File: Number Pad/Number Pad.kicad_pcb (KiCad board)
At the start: 2 copper layers, 92.9 x 95.2 mm, 42 parts, among them J1 Conn_01x19_Female, J2 Conn_01x19_Male

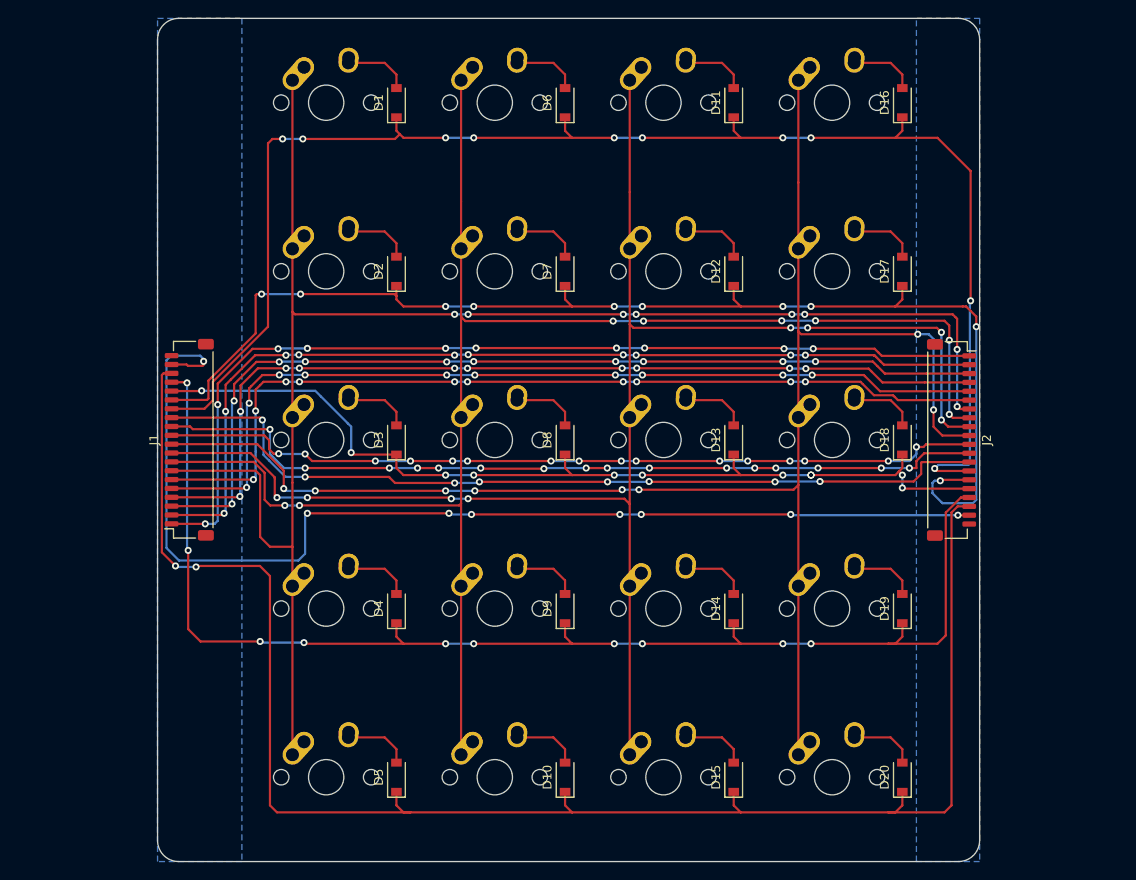
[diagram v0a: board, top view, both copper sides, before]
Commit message: Finished connectors plus mounting holes
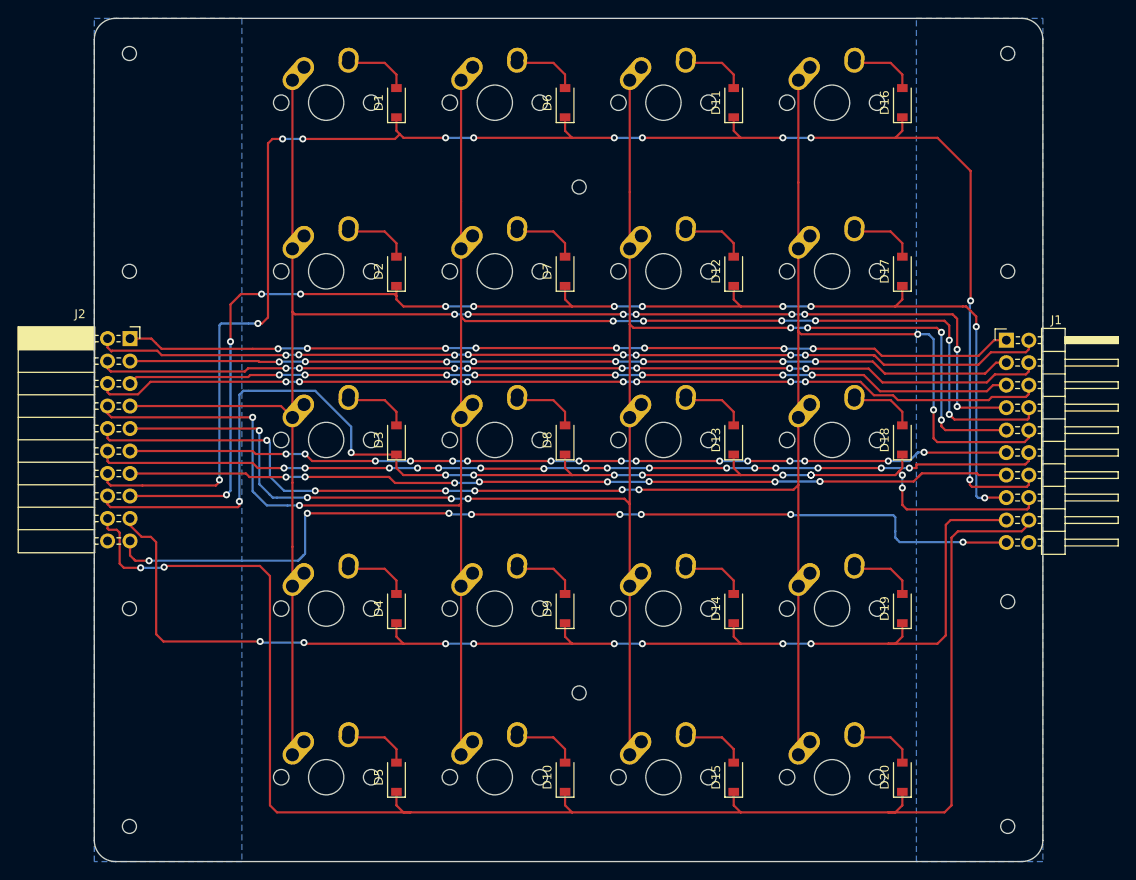
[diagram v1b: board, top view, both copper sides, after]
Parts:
- J1: value Conn_01x19_Female -> Conn_02x10_Counter_Clockwise; footprint Connector_JST:JST_SH_SM20B-SRSS-TB_1x20-1MP_P1.00mm_Horizontal -> Connector_PinHeader_2.54mm:PinHeader_2x10_P2.54mm_Horizontal
- J2: value Conn_01x19_Male -> Conn_02x10_Counter_Clockwise; footprint Connector_JST:JST_SH_SM20B-SRSS-TB_1x20-1MP_P1.00mm_Horizontal -> Connector_PinSocket_2.54mm:PinSocket_2x10_P2.54mm_Horizontal
- moved J2 93.5 mm to (27.9, 51.3), turned to 0 degrees
- moved J1 93.0 mm to (126.8, 51.4), turned to 0 degrees
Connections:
- J1 pad 20: (no net) -> unconnected-(J1-Pad20)
- J2 pad 20: (no net) -> unconnected-(J2-Pad20)
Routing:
- net ROW7: track 105.9 -> 137.1 mm
- net ROW5: track 169.5 -> 192.1 mm, vias 10 -> 12
- net COL5: track 181.1 -> 203.2 mm
- net COL7: track 180.6 -> 199.2 mm
- net GND: track 126.2 -> 109.2 mm
- net COL6: track 180.5 -> 193.4 mm
- net COL9: track 94.9 -> 107.1 mm
- net ROW6: track 141.7 -> 151.6 mm, vias 10 -> 12
- net ROW8: track 144.9 -> 135.9 mm, vias 10 -> 8
- net +5V: track 107.8 -> 100.6 mm, vias 10 -> 8
- net COL8: track 93.1 -> 99.9 mm
- net COL3: track 101.4 -> 107.9 mm, vias 10 -> 8
- net ROW9: track 185.7 -> 179.7 mm
- net COL0: track 104.9 -> 100.1 mm, vias 10 -> 8
- net COL10: track 97.1 -> 100.4 mm
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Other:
- board size 92.9 x 95.2 mm -> 107.2 x 95.2 mm

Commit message: Extended PCB for connectors
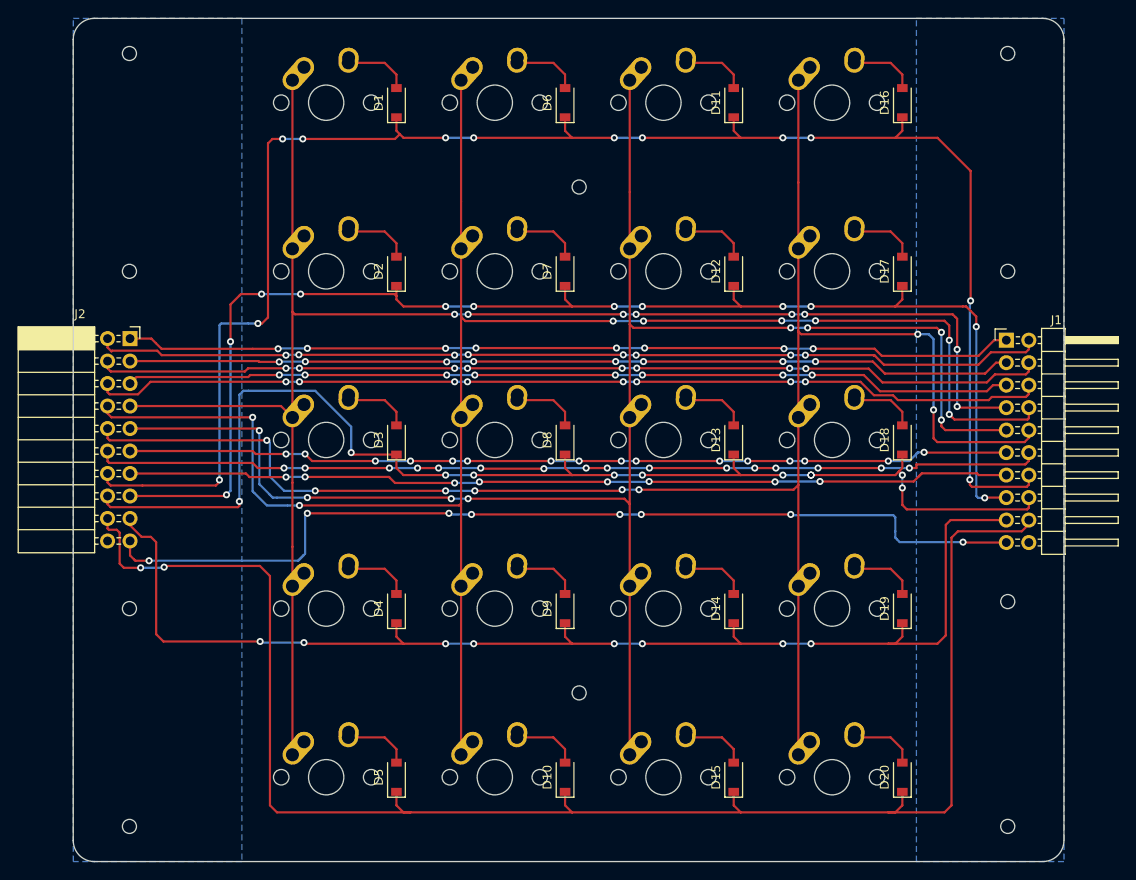
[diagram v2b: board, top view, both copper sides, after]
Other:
- board size 107.2 x 95.2 mm -> 111.9 x 95.2 mm
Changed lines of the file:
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@@
     )
   )
-  (gr_arc (start 128.5875 15.08125) (mid 130.271298 15.778702) (end 130.96875 17.4625) (layer "Edge.Cuts") (width 0.15))
   (gr_circle (center 27.78125 19.05) (end 28.575 19.05) (layer "Edge.Cuts") (width 0.1) (fill none))
   (gr_circle (center 78.58125 34.13125) (end 78.58125 33.3375) (layer "Edge.Cuts") (width 0.1) (fill none))
-  (gr_line (start 23.8125 107.95) (end 23.8125 17.4625) (layer "Edge.Cuts") (width 0.15))
-  (gr_arc (start 26.19375 110.33125) (mid 24.509952 109.633798) (end 23.8125 107.95) (layer "Edge.Cuts") (width 0.15))
-  (gr_arc (start 23.8125 17.4625) (mid 24.544321 15.74502) (end 26.289969 15.083195) (layer "Edge.Cuts") (width 0.15))
-  (gr_line (start 130.96875 107.95) (end 130.96875 17.4625) (layer "Edge.Cuts") (width 0.15))
+  (gr_line (start 21.43125 107.95) (end 21.43125 17.4625) (layer "Edge.Cuts") (width 0.15))
+  (gr_arc (start 23.8125 110.33125) (mid 22.128702 109.633798) (end 21.43125 107.95) (layer "Edge.Cuts") (width 0.15))
+  (gr_line (start 133.35 107.95) (end 133.35 17.4625) (layer "Edge.Cuts") (width 0.15))
   (gr_circle (center 27.78125 106.3625) (end 27.78125 105.56875) (layer "Edge.Cuts") (width 0.1) (fill none))
-  (gr_line (start 26.290048 15.08125) (end 128.5875 15.08125) (layer "Edge.Cuts") (width 0.15))
+  (gr_line (start 23.8125 15.08125) (end 130.96875 15.08125) (layer "Edge.Cuts") (width 0.15))
+  (gr_arc (start 130.96875 15.08125) (mid 132.652548 15.778702) (end 133.35 17.4625) (layer "Edge.Cuts") (width 0.15))
+  (gr_arc (start 21.43125 17.4625) (mid 22.128702 15.778702) (end 23.8125 15.08125) (layer "Edge.Cuts") (width 0.15))
   (gr_circle (center 127 80.9625) (end 127.79375 80.9625) (layer "Edge.Cuts") (width 0.1) (fill none))
   (gr_circle (center 27.78125 43.65625) (end 28.575 43.65625) (layer "Edge.Cuts") (width 0.1) (fill none))
   (gr_circle (center 27.78125 81.75625) (end 27.78125 80.9625) (layer "Edge.Cuts") (width 0.1) (fill none))
   (gr_circle (center 78.58125 91.28125) (end 78.58125 90.4875) (layer "Edge.Cuts") (width 0.1) (fill none))
-  (gr_arc (start 130.96875 107.95) (mid 130.271298 109.633798) (end 128.5875 110.33125) (layer "Edge.Cuts") (width 0.15))
   (gr_circle (center 127 106.3625) (end 127 105.56875) (layer "Edge.Cuts") (width 0.1) (fill none))
-  (gr_line (start 26.19375 110.33125) (end 128.5875 110.33125) (layer "Edge.Cuts") (width 0.15))
+  (gr_line (start 23.8125 110.33125) (end 130.96875 110.33125) (layer "Edge.Cuts") (width 0.15))
   (gr_circle (center 127 43.65625) (end 127 42.8625) (layer "Edge.Cuts") (width 0.1) (fill none))
   (gr_circle (center 127 19.05) (end 127 18.25625) (layer "Edge.Cuts") (width 0.1) (fill none))
+  (gr_arc (start 133.35 107.95) (mid 132.652548 109.633798) (end 130.96875 110.33125) (layer "Edge.Cuts") (width 0.151))
   (segment (start 76.99375 27.78125) (end 76.99375 26.25625) (width 0.25) (layer "F.Cu") (net 1))
   (segment (start 25.31 67.51) (end 25.55 67.75) (width 0.25) (layer "F.Cu") (net 1))
@@
       (pts
         (xy 40.48125 110.33125)
-        (xy 23.8125 110.33125)
-        (xy 23.8125 15.08125)
+        (xy 21.43125 110.33125)
+        (xy 21.43125 15.08125)
         (xy 40.48125 15.08125)
       )
@@
     (polygon
       (pts
-        (xy 130.96875 110.33125)
+        (xy 133.35 110.33125)
         (xy 116.68125 110.33125)
         (xy 116.68125 15.08125)
-        (xy 130.96875 15.08125)
+        (xy 133.35 15.08125)
       )
     )
